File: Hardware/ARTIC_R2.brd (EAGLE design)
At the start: 22.9 x 50.8 mm, 142 parts, among them J1 U.FL, J2 THING_PLUS, J5 Flash Programming, K1 TLP3475R, Q1 3.1A/30V/105mΩ, U1 2Mbit SPI Flash, U2 1.8V/100mA, U3 ARTIC_R2, U4 RFPA0133, U5 AS179-92LF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

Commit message: Changing R7 from 10K to 1K
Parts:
- R7: value 10k -> 1k
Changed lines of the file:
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@@
 <attribute name="PROD_ID" value="NDUC-15277" x="11.43" y="32.639" size="1.778" layer="27" ratio="15" rot="R90" display="off"/>
 </element>
-<element name="R7" library="SparkFun-Resistors" package="0402-TIGHT" value="10k" x="5.715" y="39.6875" smashed="yes" rot="R270">
+<element name="R7" library="SparkFun-Resistors" package="0402-TIGHT" value="1k" x="5.715" y="39.6875" smashed="yes" rot="R270">
 <attribute name="NAME" x="6.277" y="39.6875" size="0.6096" layer="25" font="vector" ratio="20" rot="R270" align="bottom-center"/>
-<attribute name="PROD_ID" value="RES-14241" x="5.715" y="39.6875" size="1.778" layer="27" ratio="15" rot="R270" display="off"/>
+<attribute name="PROD_ID" value="RES-14342" x="5.715" y="39.6875" size="1.778" layer="27" ratio="15" rot="R270" display="off"/>
 </element>
 <element name="C23" library="SparkFun-Capacitors" package="0402-TIGHT" value="100pF" x="8.5725" y="39.6875" smashed="yes" rot="R270">

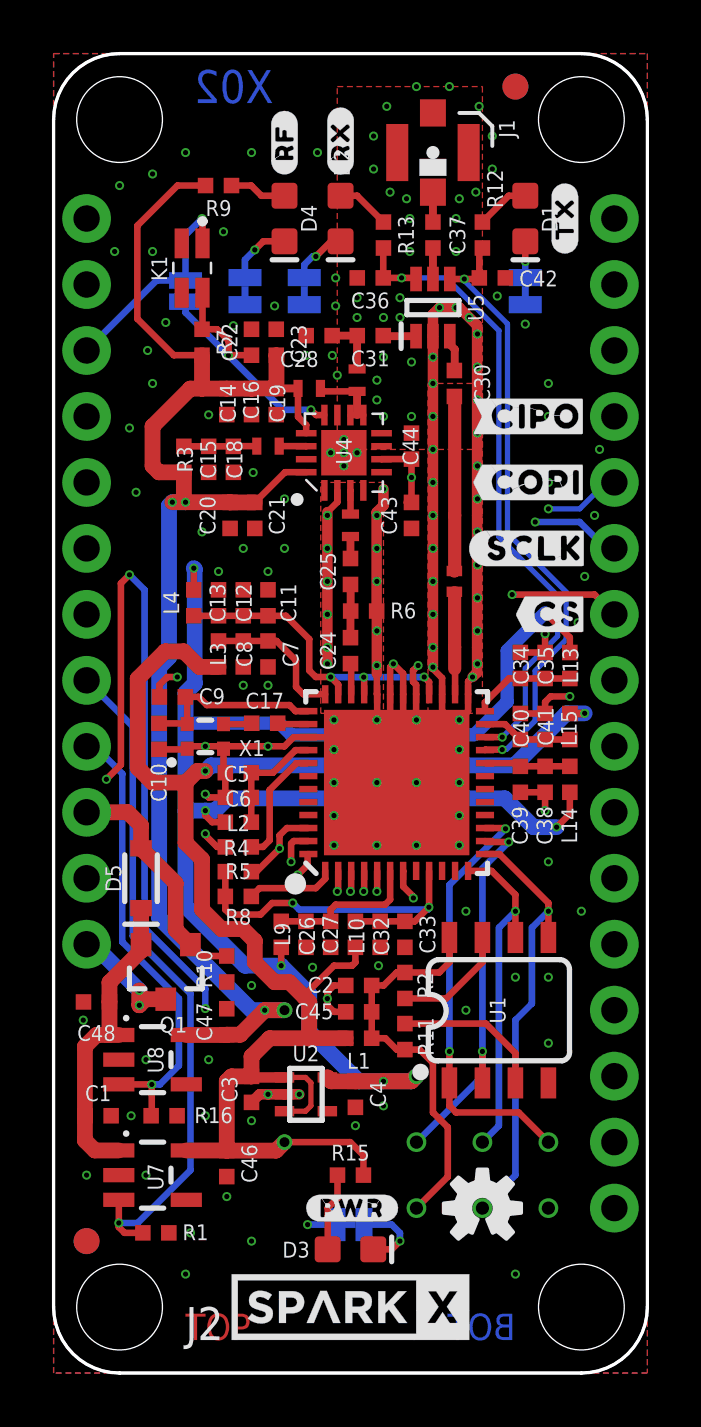
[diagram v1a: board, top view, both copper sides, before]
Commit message: Updates for X03. Design now includes a 3.0V regulator for the RF amp gain and bias.
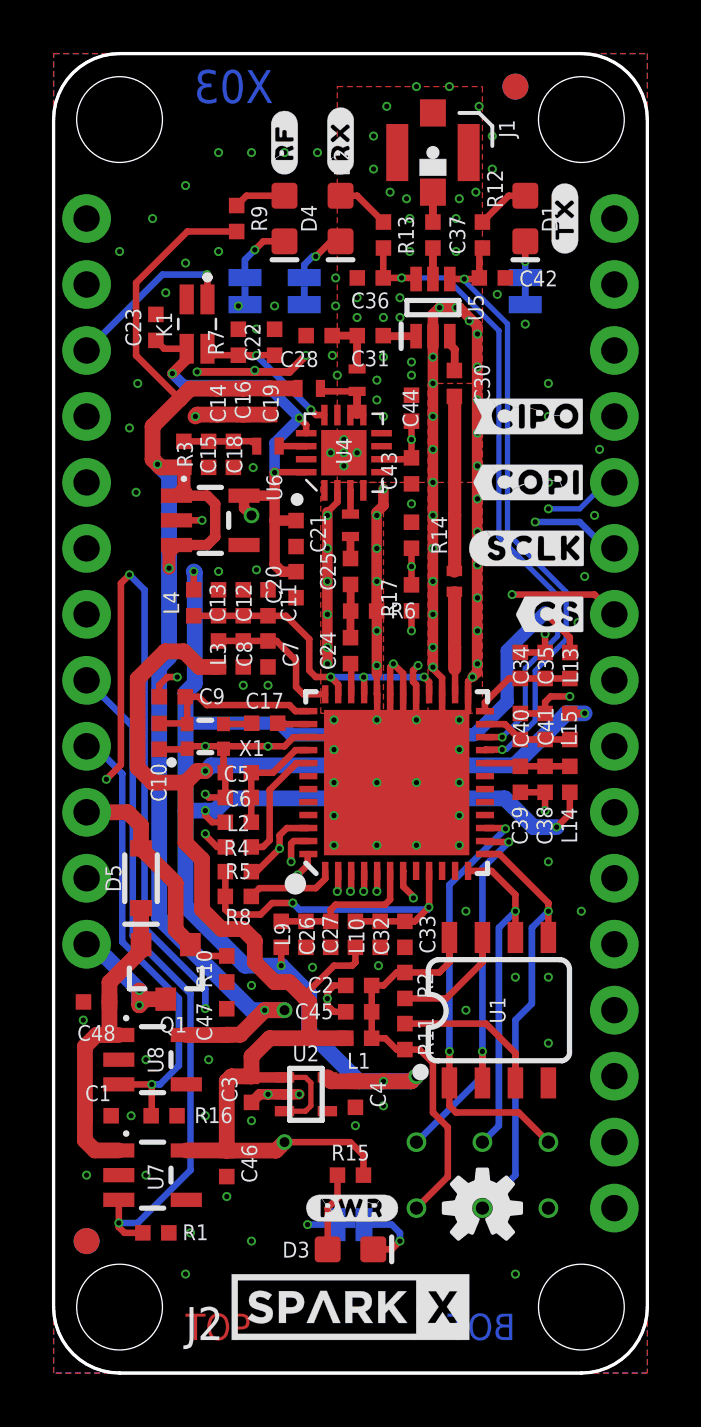
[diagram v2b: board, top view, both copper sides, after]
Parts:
- removed JP7: JUMPER-SMT_2_NO_SILK, SparkFun-Jumpers:SMT-JUMPER_2_NO_SILK
- removed U$22: (no value), output:##8DB#0
- added R14: 470, New_Parts_Resistors:0402-TIGHT
- added R17: 47, New_Parts_Resistors:0402-TIGHT
- added TP4: TEST-POINTTP_15TH_THRU, SparkFun-Connectors:TP_15TH
- added U6: 3.0V, New_Parts_IC-Power:SOT23-5
- R1, R16: value 100k -> 10k
- R7: value 1k -> 10k
- U$6: device output:#GAIN8#0 -> output:#8DB#0
- moved U$6 6.10 mm to (4.19, 39.4), turned to 0 degrees
- moved C23 4.67 mm to (3.94, 40.3), turned to 90 degrees
- moved C20 3.68 mm to (9.33, 30.4)
- moved K1 2.17 mm to (5.52, 40.4)
- moved C21 1.73 mm to (9.33, 32.3)
- moved C43 1.71 mm to (13.8, 34.7)
- moved C44 1.46 mm to (13.8, 37.1)
- moved R9 1.45 mm to (7.05, 44.5), turned to 270 degrees
- moved R7 1.40 mm to (7.11, 39.7), turned to 90 degrees
- moved C22 0.89 mm to (8.51, 39.7)
- moved C14 0.38 mm to (6.29, 37.4)
- moved C16 0.32 mm to (7.30, 37.4)
- moved C19 0.25 mm to (8.32, 37.4)
- moved C15 0.19 mm to (5.97, 35.4)
- moved C18 0.19 mm to (6.92, 35.4)
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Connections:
- new net PD: C43.2, C44.1, R14.2, R17.2, U4.6
- new net VREF1: C20.2, C21.2, C23.1, K1.3, TP4.P$1, U4.13, U4.16, U6.5
- net G8: no longer JP7.1
- net GND: now also C23.2, R14.1, R7.2, U6.2; no longer C23.1, K1.3
- net PA_PD: now also R17.1; no longer C43.2, C44.1, U4.6
- net RFG8: no longer JP7.2
- net VDDA: now also U6.1, U6.3; no longer C20.2, C21.2, C23.2, R7.2, U4.13, U4.16
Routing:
- net VREF1: track 0.00 -> 19.9 mm, vias 0 -> 3
- net PD: track 0.00 -> 9.51 mm, vias 0 -> 2
- net GND: track 106.6 -> 115.0 mm, vias 168 -> 170
- net PA_PD: track 25.3 -> 17.2 mm
- net RFG8: track 11.5 -> 6.27 mm
- net VDDA: track 57.4 -> 53.7 mm
- net G8: track 8.54 -> 6.81 mm
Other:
- board text added: "X03"
- board text removed: "X02"

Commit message: Final tweaks for X03. Changed 8dB to G8. Increased annular ring to 3.5mil.
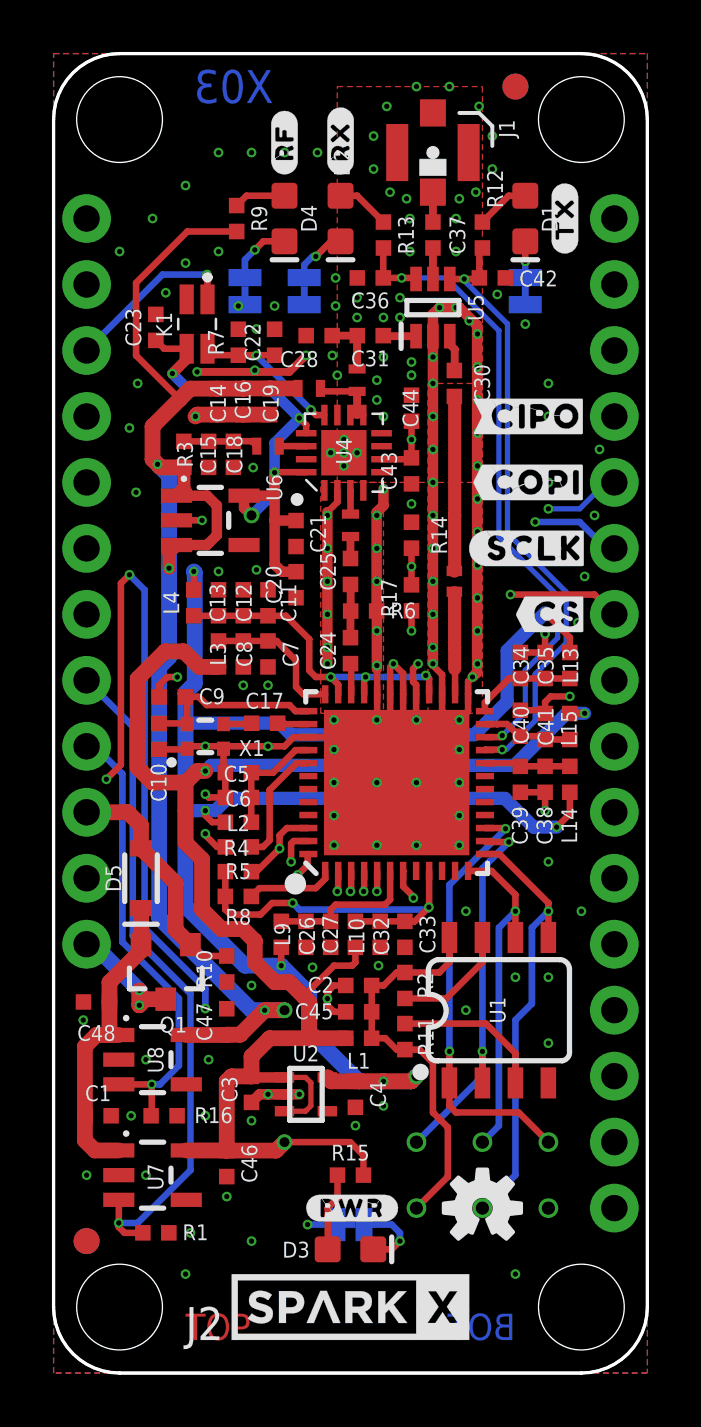
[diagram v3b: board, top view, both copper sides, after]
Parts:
- U$6: device output:#8DB#0 -> output:#G8#0
- moved U$6 0.38 mm to (3.81, 39.4)
- moved C40 0.13 mm to (18.0, 25.0)
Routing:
- net VREF1: track 19.9 -> 21.9 mm
